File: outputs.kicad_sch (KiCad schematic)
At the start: 56 parts, among them Q2 DTC113Z, Q3 DTC113Z, Q4 DTC113Z, Q5 DTC113Z, Q6 DTC113Z, Q7 DTC113Z, Q8 DTC113Z, Q9 DTC113Z, U10 AQH0213, U11 AQH0213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

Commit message: changes for layout
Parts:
- F1, F2, F3, F4, F5, F6, F7, F8: footprint Varistor:RV_Disc_D7mm_W3.4mm_P5mm -> Capacitor_THT:C_Disc_D8.0mm_W5.0mm_P5.00mm
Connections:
- net GND: now also Q2.2 (E), Q3.2 (E), Q6.2 (E), Q7.2 (E)
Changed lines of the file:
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@@
     (property "Reference" "F3" (id 0) (at 105.41 105.41 90))
     (property "Value" "500mA" (id 1) (at 107.95 107.95 90))
-    (property "Footprint" "Varistor:RV_Disc_D7mm_W3.4mm_P5mm" (id 2) (at 106.68 104.648 90)
+    (property "Footprint" "Capacitor_THT:C_Disc_D8.0mm_W5.0mm_P5.00mm" (id 2) (at 106.68 104.648 90)
       (effects (font (size 1.27 1.27)) hide)
     )
@@
     (property "Reference" "F5" (id 0) (at 213.36 137.16 90))
     (property "Value" "500mA" (id 1) (at 215.9 139.7 90))
-    (property "Footprint" "Varistor:RV_Disc_D7mm_W3.4mm_P5mm" (id 2) (at 214.63 136.398 90)
+    (property "Footprint" "Capacitor_THT:C_Disc_D8.0mm_W5.0mm_P5.00mm" (id 2) (at 214.63 136.398 90)
       (effects (font (size 1.27 1.27)) hide)
     )
@@
     (pin "1")
   )
+  (symbol (lib_name "GND_1") (lib_id "power:GND") (at 71.12 148.59 0) (unit 1)
+    (in_bom yes) (on_board yes) (fields_autoplaced)
+    (property "Reference" "#PWR0103" (id 0) (at 71.12 154.94 0)
+      (effects (font (size 1.27 1.27)) hide)
+    )
+    (property "Value" "GND" (id 1) (at 68.58 149.8601 0)
+      (effects (font (size 1.27 1.27)) (justify right) hide)
+    )
+    (property "Footprint" "" (id 2) (at 71.12 148.59 0)
+      (effects (font (size 1.27 1.27)) hide)
+    )
+    (property "Datasheet" "" (id 3) (at 71.12 148.59 0)
+      (effects (font (size 1.27 1.27)) hide)
+    )
+    (pin "1")
+  )
   (symbol (lib_id "power:+5V") (at 62.23 90.17 0) (unit 1)
     (in_bom yes) (on_board yes) (fields_autoplaced)
@@
     (pin "1")
     (pin "2")
+  )
+  (symbol (lib_name "GND_1") (lib_id "power:GND") (at 180.34 148.59 0) (unit 1)
+    (in_bom yes) (on_board yes) (fields_autoplaced)
+    (property "Reference" "#PWR0105" (id 0) (at 180.34 154.94 0)
+      (effects (font (size 1.27 1.27)) hide)
+    )
+    (property "Value" "GND" (id 1) (at 177.8 149.8601 0)
+      (effects (font (size 1.27 1.27)) (justify right) hide)
+    )
+    (property "Footprint" "" (id 2) (at 180.34 148.59 0)
+      (effects (font (size 1.27 1.27)) hide)
+    )
+    (property "Datasheet" "" (id 3) (at 180.34 148.59 0)
+      (effects (font (size 1.27 1.27)) hide)
+    )
+    (pin "1")
   )
   (symbol (lib_id "Device:R_Small_US") (at 170.18 125.73 0) (mirror y) (unit 1)
@@
     (pin "3")
   )
+  (symbol (lib_name "GND_1") (lib_id "power:GND") (at 72.39 85.09 0) (unit 1)
+    (in_bom yes) (on_board yes) (fields_autoplaced)
+    (property "Reference" "#PWR0102" (id 0) (at 72.39 91.44 0)
+      (effects (font (size 1.27 1.27)) hide)
+    )
+    (property "Value" "GND" (id 1) (at 69.85 86.3601 0)
+      (effects (font (size 1.27 1.27)) (justify right) hide)
+    )
+    (property "Footprint" "" (id 2) (at 72.39 85.09 0)
+      (effects (font (size 1.27 1.27)) hide)
+    )
+    (property "Datasheet" "" (id 3) (at 72.39 85.09 0)
+      (effects (font (size 1.27 1.27)) hide)
+    )
+    (pin "1")
+  )
   (symbol (lib_id "Device:R_Small_US") (at 60.96 125.73 0) (mirror y) (unit 1)
     (in_bom yes) (on_board yes)
@@
     (pin "1")
     (pin "2")
+  )
+  (symbol (lib_name "GND_1") (lib_id "power:GND") (at 181.61 85.09 0) (unit 1)
+    (in_bom yes) (on_board yes) (fields_autoplaced)
+    (property "Reference" "#PWR0104" (id 0) (at 181.61 91.44 0)
+      (effects (font (size 1.27 1.27)) hide)
+    )
+    (property "Value" "GND" (id 1) (at 179.07 86.3601 0)
+      (effects (font (size 1.27 1.27)) (justify right) hide)
+    )
+    (property "Footprint" "" (id 2) (at 181.61 85.09 0)
+      (effects (font (size 1.27 1.27)) hide)
+    )
+    (property "Datasheet" "" (id 3) (at 181.61 85.09 0)
+      (effects (font (size 1.27 1.27)) hide)
+    )
+    (pin "1")
   )
   (symbol (lib_id "Transistor_BJT:DTC113Z") (at 179.07 80.01 0) (unit 1)
@@
     (property "Reference" "F2" (id 0) (at 105.41 73.66 90))
     (property "Value" "500mA" (id 1) (at 107.95 76.2 90))
-    (property "Footprint" "Varistor:RV_Disc_D7mm_W3.4mm_P5mm" (id 2) (at 106.68 72.898 90)
+    (property "Footprint" "Capacitor_THT:C_Disc_D8.0mm_W5.0mm_P5.00mm" (id 2) (at 106.68 72.898 90)
       (effects (font (size 1.27 1.27)) hide)
     )
@@
     (property "Reference" "F8" (id 0) (at 215.9 41.91 90))
     (property "Value" "500mA" (id 1) (at 218.44 44.45 90))
-    (property "Footprint" "Varistor:RV_Disc_D7mm_W3.4mm_P5mm" (id 2) (at 217.17 41.148 90)
+    (property "Footprint" "Capacitor_THT:C_Disc_D8.0mm_W5.0mm_P5.00mm" (id 2) (at 217.17 41.148 90)
       (effects (font (size 1.27 1.27)) hide)
     )
@@
     (property "Reference" "F1" (id 0) (at 104.14 137.16 90))
     (property "Value" "500mA" (id 1) (at 106.68 139.7 90))
-    (property "Footprint" "Varistor:RV_Disc_D7mm_W3.4mm_P5mm" (id 2) (at 105.41 136.398 90)
+    (property "Footprint" "Capacitor_THT:C_Disc_D8.0mm_W5.0mm_P5.00mm" (id 2) (at 105.41 136.398 90)
       (effects (font (size 1.27 1.27)) hide)
     )
@@
     (property "Reference" "F6" (id 0) (at 214.63 73.66 90))
     (property "Value" "500mA" (id 1) (at 217.17 76.2 90))
-    (property "Footprint" "Varistor:RV_Disc_D7mm_W3.4mm_P5mm" (id 2) (at 215.9 72.898 90)
+    (property "Footprint" "Capacitor_THT:C_Disc_D8.0mm_W5.0mm_P5.00mm" (id 2) (at 215.9 72.898 90)
       (effects (font (size 1.27 1.27)) hide)
     )
@@
     (property "Reference" "F7" (id 0) (at 214.63 105.41 90))
     (property "Value" "500mA" (id 1) (at 217.17 107.95 90))
-    (property "Footprint" "Varistor:RV_Disc_D7mm_W3.4mm_P5mm" (id 2) (at 215.9 104.648 90)
+    (property "Footprint" "Capacitor_THT:C_Disc_D8.0mm_W5.0mm_P5.00mm" (id 2) (at 215.9 104.648 90)
       (effects (font (size 1.27 1.27)) hide)
     )
@@
     (property "Reference" "F4" (id 0) (at 106.68 41.91 90))
     (property "Value" "500mA" (id 1) (at 109.22 44.45 90))
-    (property "Footprint" "Varistor:RV_Disc_D7mm_W3.4mm_P5mm" (id 2) (at 107.95 41.148 90)
-      (effects (font (size 1.27 1.27)) hide)
-    )
+    (property "Footprint" "Capacitor_THT:C_Disc_D8.0mm_W5.0mm_P5.00mm" (id 2) (at 107.95 41.148 90)
+      (effects (font (size 1.27 1.27)) hide)
+    )

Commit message: added some part numbers
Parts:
- OUT_0, OUT_1, OUT_2, OUT_3, OUT_4, OUT_5, OUT_6, OUT_7: Digikey (none) -> A113320-ND
- U10, U11, U12, U13, U14, U7, U8, U9: Digikey (none) -> 255-5987-ND
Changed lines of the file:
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@@
+      (effects (font (size 1.27 1.27)) hide)
+    )
+    (property "Digikey" "A113320-ND" (id 4) (at 125.73 68.58 0)
       (effects (font (size 1.27 1.27)) hide)
     )
@@
     )
     (property "Datasheet" "~" (id 3) (at 234.95 100.33 0)
+      (effects (font (size 1.27 1.27)) hide)
+    )
+    (property "Digikey" "A113320-ND" (id 4) (at 234.95 100.33 0)
       (effects (font (size 1.27 1.27)) hide)
     )
@@
       (effects (font (size 1.27 1.27)) (justify left) hide)
     )
+    (property "Digikey" "255-5987-ND" (id 4) (at 194.31 36.83 0)
+      (effects (font (size 1.27 1.27)) hide)
+    )
     (pin "1")
     (pin "2")
@@
       (effects (font (size 1.27 1.27)) (justify left) hide)
     )
+    (property "Digikey" "255-5987-ND" (id 4) (at 83.82 100.33 0)
+      (effects (font (size 1.27 1.27)) hide)
+    )
     (pin "1")
     (pin "2")
@@
       (effects (font (size 1.27 1.27)) hide)
     )
+    (property "Digikey" "A113320-ND" (id 4) (at 236.22 36.83 0)
+      (effects (font (size 1.27 1.27)) hide)
+    )
     (pin "1")
     (pin "2")
@@
       (effects (font (size 1.27 1.27)) hide)
     )
+    (property "Digikey" "A113320-ND" (id 4) (at 233.68 132.08 0)
+      (effects (font (size 1.27 1.27)) hide)
+    )
     (pin "1")
     (pin "2")
@@
     )
     (property "Datasheet" "~" (id 3) (at 124.46 132.08 0)
+      (effects (font (size 1.27 1.27)) hide)
+    )
+    (property "Digikey" "A113320-ND" (id 4) (at 124.46 132.08 0)
       (effects (font (size 1.27 1.27)) hide)
     )
@@
       (effects (font (size 1.27 1.27)) (justify left) hide)
     )
+    (property "Digikey" "255-5987-ND" (id 4) (at 191.77 132.08 0)
+      (effects (font (size 1.27 1.27)) hide)
+    )
     (pin "1")
     (pin "2")
@@
       (effects (font (size 1.27 1.27)) (justify left) hide)
     )
+    (property "Digikey" "255-5987-ND" (id 4) (at 85.09 36.83 0)
+      (effects (font (size 1.27 1.27)) hide)
+    )
     (pin "1")
     (pin "2")
@@
       (effects (font (size 1.27 1.27)) (justify left) hide)
     )
+    (property "Digikey" "255-5987-ND" (id 4) (at 193.04 100.33 0)
+      (effects (font (size 1.27 1.27)) hide)
+    )
     (pin "1")
     (pin "2")
@@
       (effects (font (size 1.27 1.27)) (justify left) hide)
     )
+    (property "Digikey" "255-5987-ND" (id 4) (at 193.04 68.58 0)
+      (effects (font (size 1.27 1.27)) hide)
+    )
     (pin "1")
     (pin "2")
@@
       (effects (font (size 1.27 1.27)) hide)
     )
+    (property "Digikey" "A113320-ND" (id 4) (at 125.73 100.33 0)
+      (effects (font (size 1.27 1.27)) hide)
+    )
     (pin "1")
     (pin "2")
@@
       (effects (font (size 1.27 1.27)) (justify left) hide)
     )
+    (property "Digikey" "255-5987-ND" (id 4) (at 82.55 132.08 0)
+      (effects (font (size 1.27 1.27)) hide)
+    )
     (pin "1")
     (pin "2")
@@
       (effects (font (size 1.27 1.27)) (justify left) hide)
     )
+    (property "Digikey" "255-5987-ND" (id 4) (at 83.82 68.58 0)
+      (effects (font (size 1.27 1.27)) hide)
+    )
     (pin "1")
     (pin "2")
@@
       (effects (font (size 1.27 1.27)) hide)
     )
+    (property "Digikey" "A113320-ND" (id 4) (at 234.95 68.58 0)
+      (effects (font (size 1.27 1.27)) hide)
+    )
     (pin "1")
     (pin "2")
@@
       (effects (font (size 1.27 1.27)) hide)
     )
+    (property "Digikey" "A113320-ND" (id 4) (at 127 36.83 0)
+      (effects (font (size 1.27 1.27)) hide)
+    )

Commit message: add copyright notices
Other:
- note added: "Copyright (C) 2023"
- note added: "Jonathan Bagg"
- note added: "SOLAR CONTROLLER 2023 - Solid State Relay Outputs"
- note added: "See https://creativecommons.org/licenses/by-nc-sa/4.0/"
- note added: "v1"

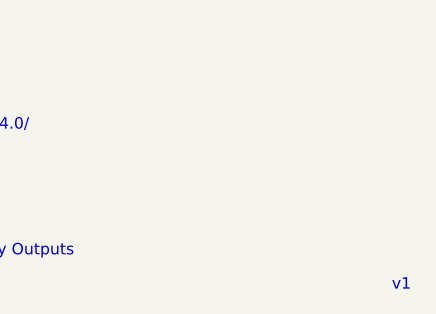
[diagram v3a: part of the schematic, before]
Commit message: AC couple LMT01 signal conditioning and add gain
The difference circuit U3A was DC coupled and so could not
have gain.  Unit gain was only good for sensors up to 15m of
cat-5.
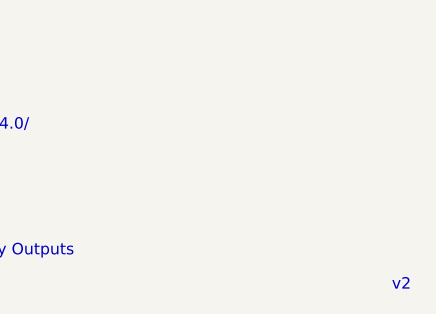
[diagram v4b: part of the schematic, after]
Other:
- note added: "v2"
- note removed: "v1"
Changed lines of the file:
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@@
     (effects (font (size 1.27 1.27)) (justify left bottom))
   )
-  (text "v1" (at 271.78 194.31 0)
+  (text "v2" (at 271.78 194.31 0)
     (effects (font (size 1.27 1.27)) (justify left bottom))
   )
